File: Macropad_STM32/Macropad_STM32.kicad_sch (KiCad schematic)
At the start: 28 parts, among them J1 USB_C_Receptacle_USB2.0, J2 Conn_01x04_Pin, SW1 SW_Push, U1 STM32F103C8T6, U3 AMS1117-3.3, Y1 16MHz

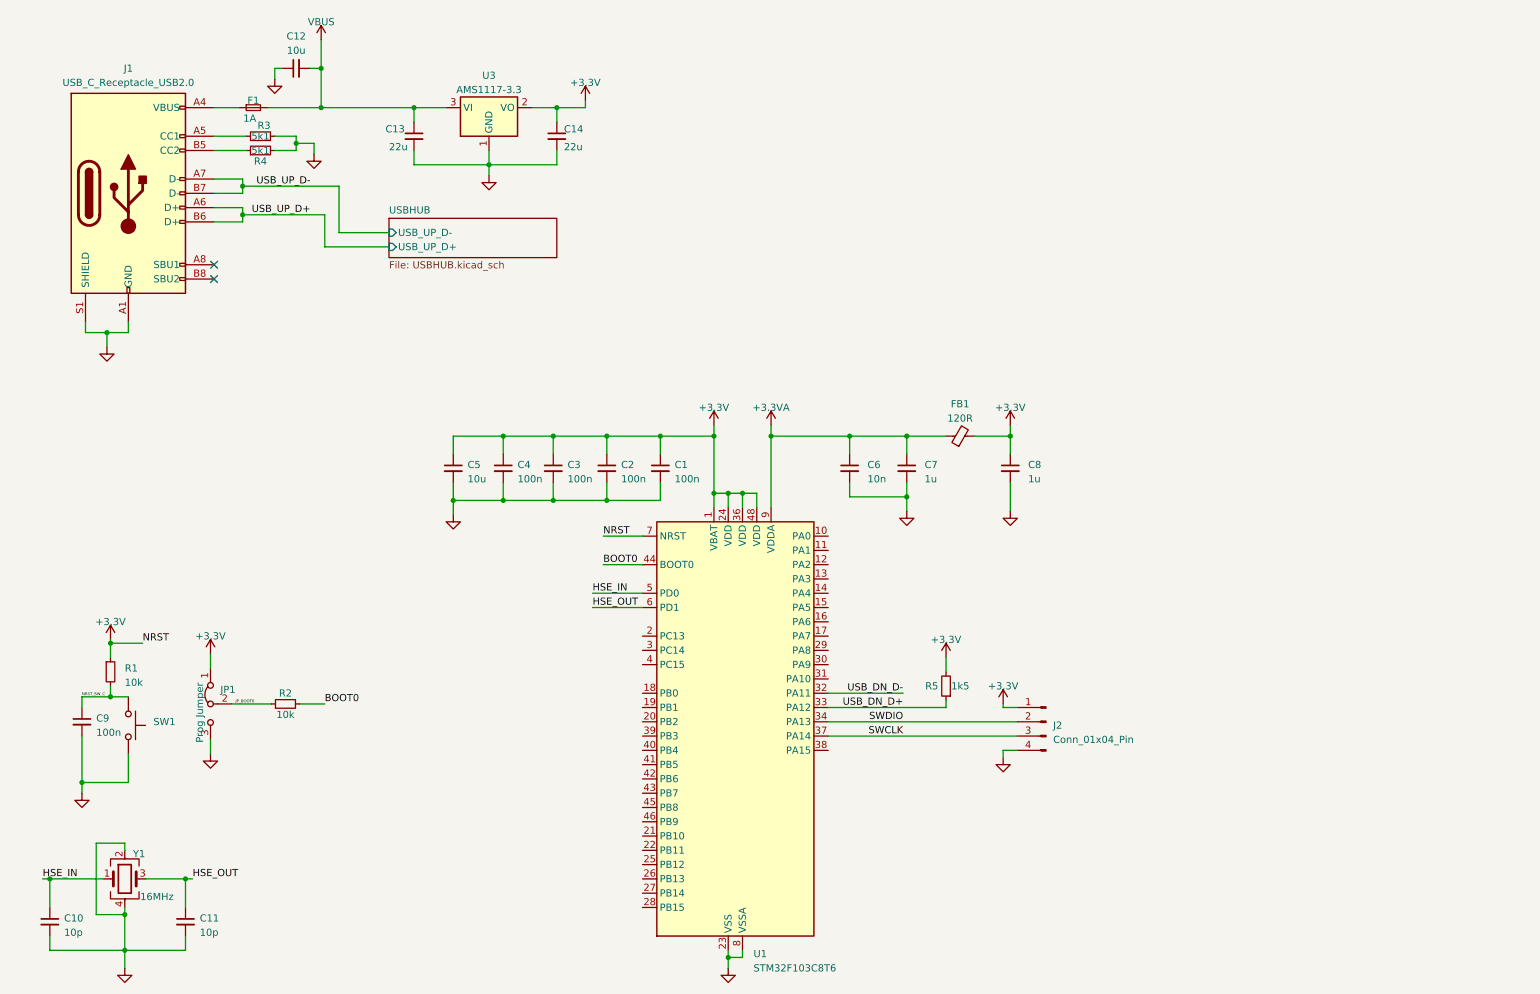
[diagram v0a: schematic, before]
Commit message: USB Hub & Jtag connectors added Todo: - Keypad matrix - Rotary encoders - PCB
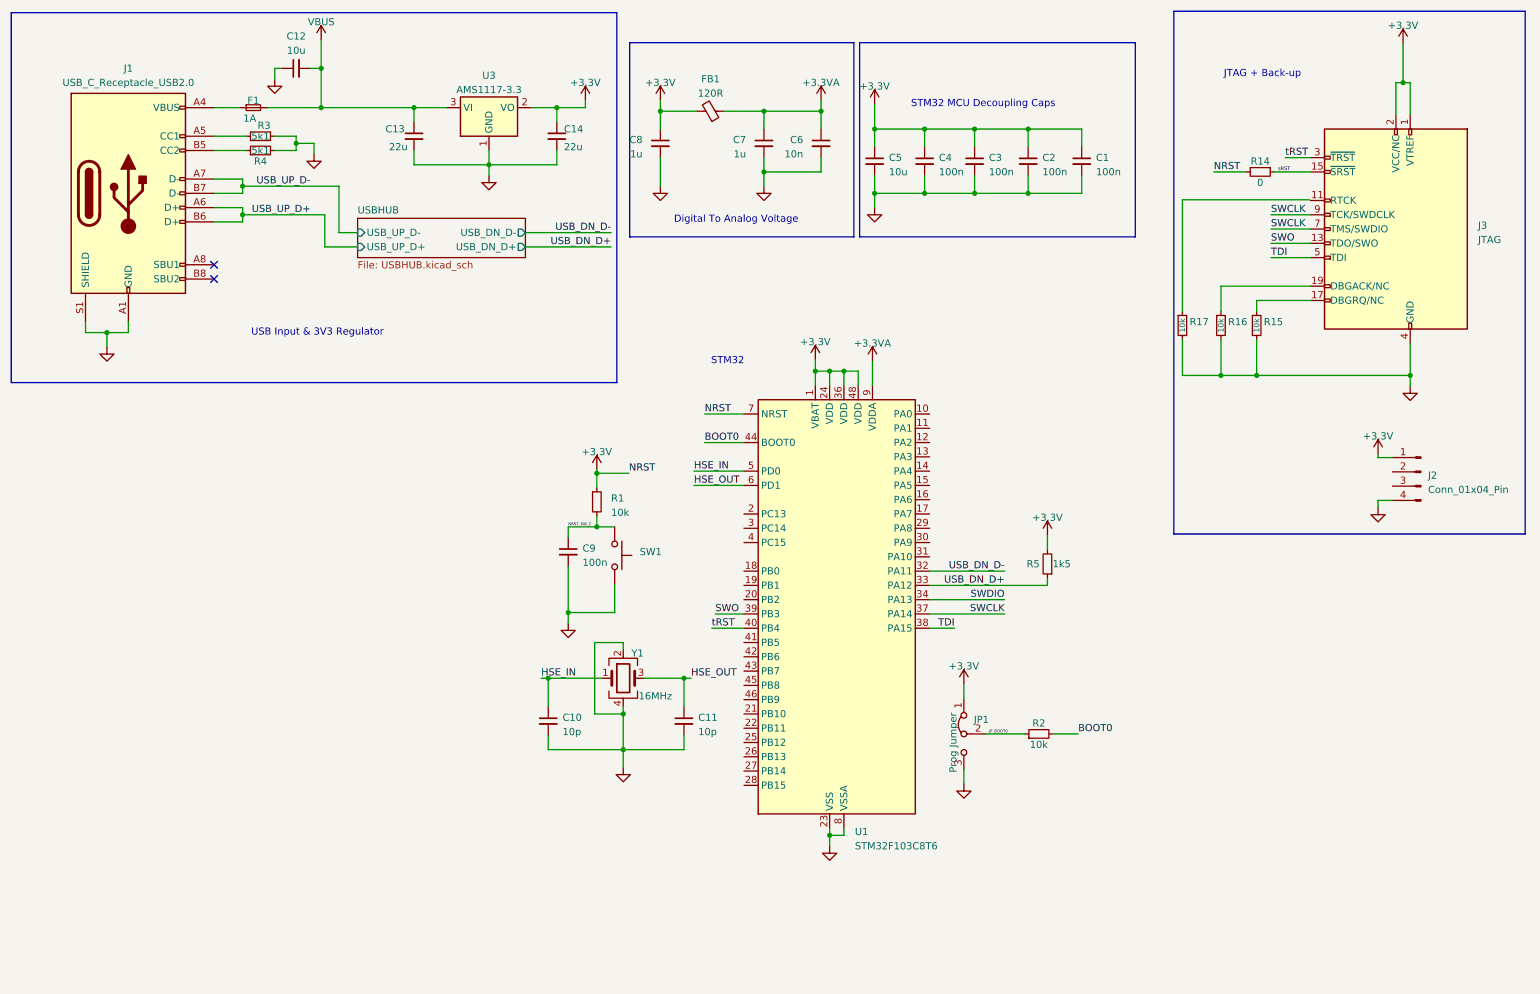
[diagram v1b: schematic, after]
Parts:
- added J3: JTAG, symbol Connector:Conn_ARM_JTAG_SWD_20
- added R14: 0, symbol Device:R_Small
- added R15, R16, R17: 10k, symbol Device:R_Small
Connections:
- net +3.3V: now also J3.1 (VTREF), J3.2 (VCC/NC), R14.2
- net GND: now also J3.10 (GND), J3.12 (GND), J3.14 (GND), J3.16 (GND), J3.18 (GND), J3.20 (GND), J3.4 (GND), J3.6 (GND), J3.8 (GND), R15.2, R16.2, R17.2
- net SWCLK: now also J3.7 (TMS/SWDIO), J3.9 (TCK/SWDCLK); no longer J2.3 (Pin_3)
- net SWDIO: no longer J2.2 (Pin_2)
- net TDI: now reaches U1.38 (PA15)
- net TDI: now also J3.5 (TDI)
- net SWO: now reaches U1.39 (PB3)
- net SWO: now also J3.13 (TDO/SWO)
- net tRST: now reaches U1.40 (PB4)
- net tRST: now also J3.3 (~{TRST})
- new net: J3.17 (DBGRQ/NC), R15.1
- new net: J3.19 (DBGACK/NC), R16.1
- new net sRST: J3.15 (~{SRST}), R14.1
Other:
- sheet USBHUB ports: added USB_DN_D+, USB_DN_D-; removed none
- note added: "Digital To Analog Voltage"
- note added: "JTAG + Back-up"
- note added: "STM32"
- note added: "STM32 MCU Decoupling Caps"
- note added: "USB Input & 3V3 Regulator"
- moved on the sheet: C1, C10, C11, C2, C3, C4, C5, C6, C7, C8, C9, FB1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

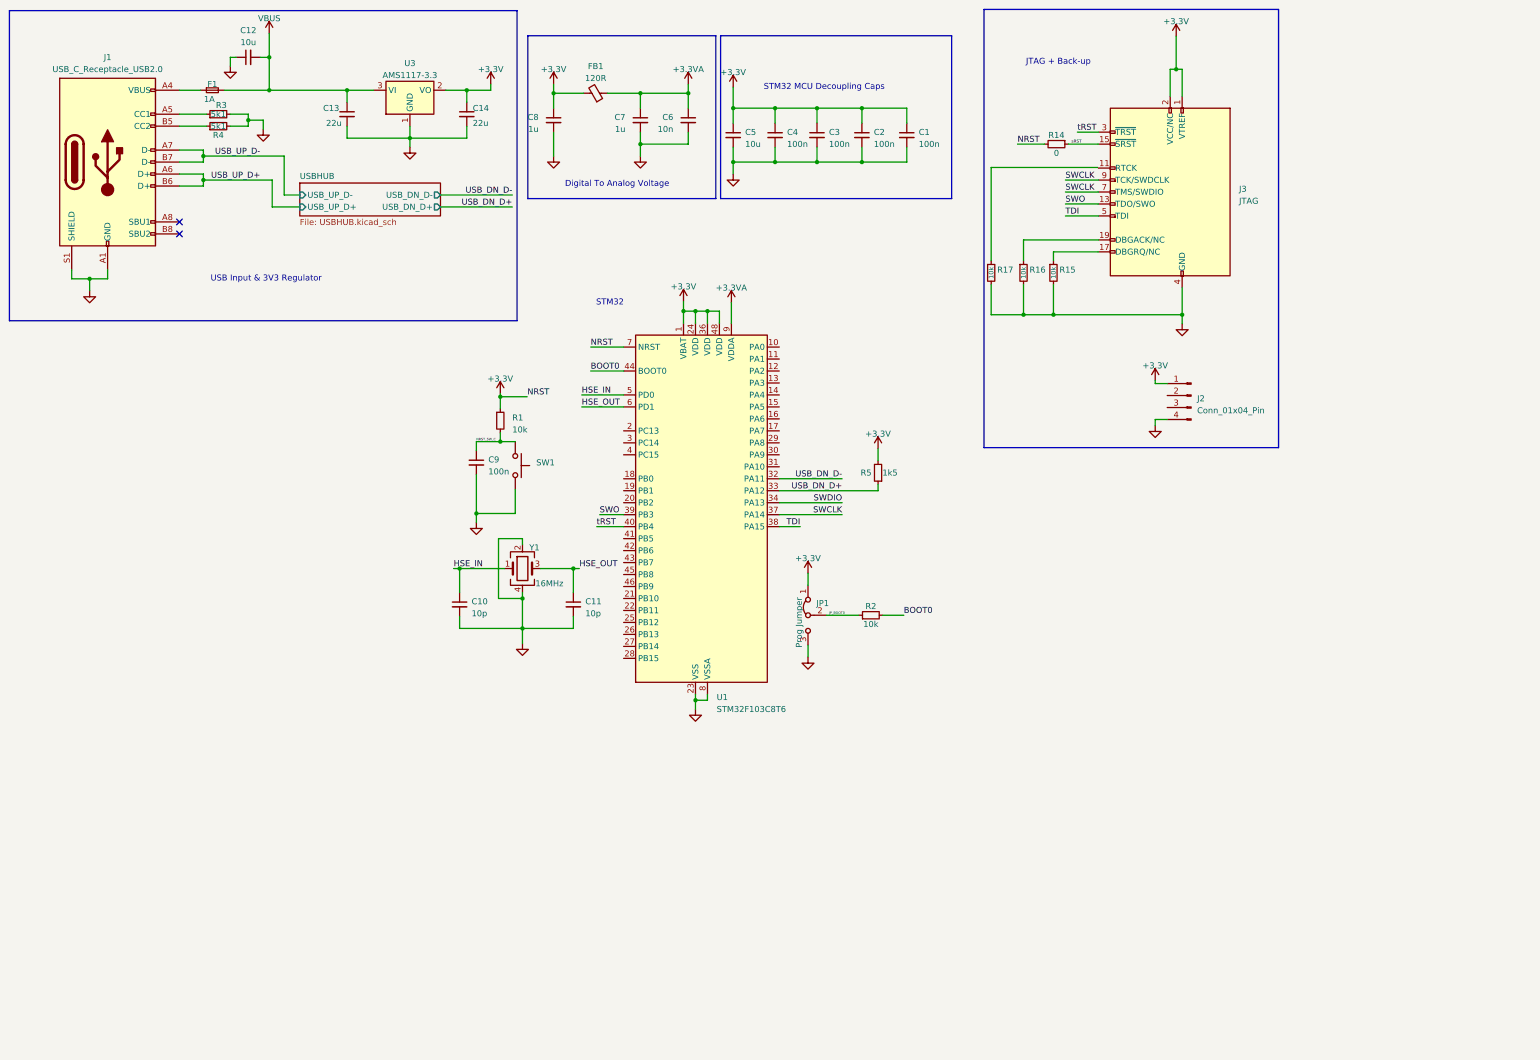
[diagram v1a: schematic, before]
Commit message: Finished main schematic (excl. matrix)
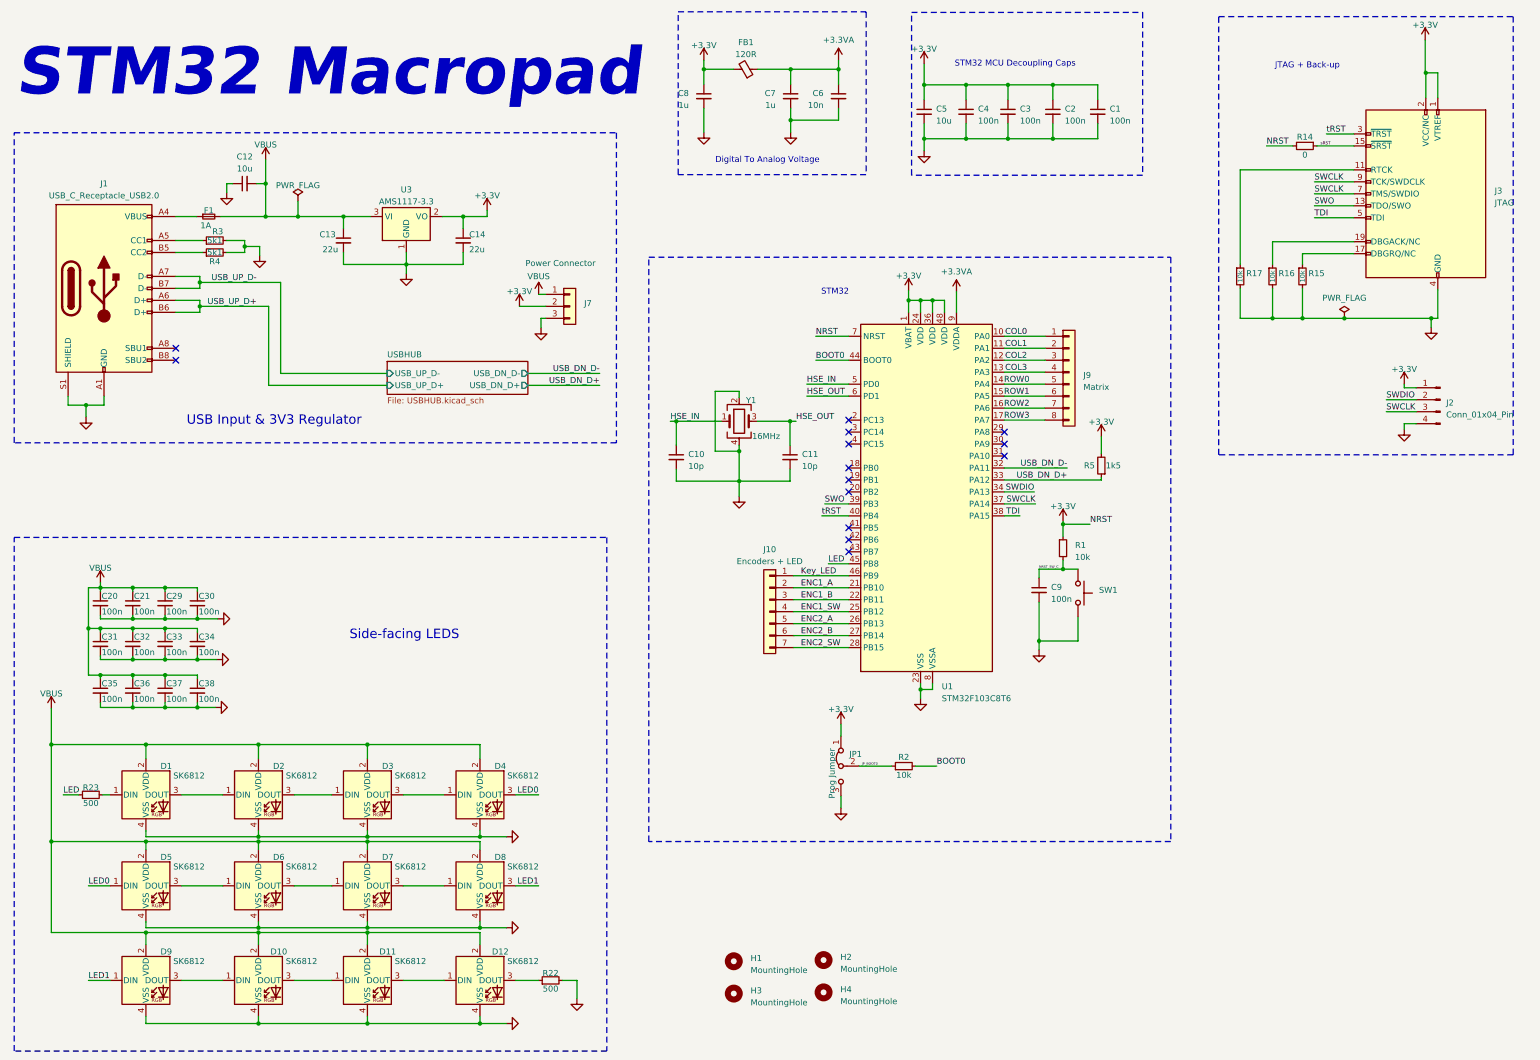
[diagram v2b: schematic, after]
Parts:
- added C20, C21, C29, C30, C31, C32, C33, C34, C35, C36, C37, C38: 100n, Capacitor_SMD:C_0805_2012Metric_Pad1.18x1.45mm_HandSolder, symbol Device:C_Small
- added D1, D10, D11, D12, D2, D3, D4, D5, D6, D7, D8, D9: SK6812, SK6812SIDE:SK6812SIDE, symbol LED:SK6812
- added H1, H2, H3, H4: MountingHole, MountingHole:MountingHole_3.2mm_M3_DIN965, symbol Mechanical:MountingHole
- added J10: Encoders + LED, Connector_JST:JST_EH_B7B-EH-A_1x07_P2.50mm_Vertical, symbol Connector_Generic:Conn_01x07
- added J7: Power Connector, Connector_JST:JST_EH_B3B-EH-A_1x03_P2.50mm_Vertical, symbol Connector_Generic:Conn_01x03
- added J9: Matrix, Connector_JST:JST_EH_B8B-EH-A_1x08_P2.50mm_Vertical, symbol Connector_Generic:Conn_01x08
- added R22, R23: 500, Resistor_SMD:R_0805_2012Metric_Pad1.20x1.40mm_HandSolder, symbol Device:R_Small
- C1, C10, C11, C12, C13, C14, C2, C3, C4, C5, C6, C7, C8, C9: footprint (none) -> Capacitor_SMD:C_0805_2012Metric_Pad1.18x1.45mm_HandSolder
- F1: footprint (none) -> Fuse:Fuse_1206_3216Metric_Pad1.42x1.75mm_HandSolder
- FB1: footprint (none) -> Fuse:Fuse_0805_2012Metric_Pad1.15x1.40mm_HandSolder
- J1: footprint (none) -> Connector_USB:USB_C_Receptacle_HRO_TYPE-C-31-M-12
- J2: footprint (none) -> Connector_PinHeader_2.54mm:PinHeader_1x04_P2.54mm_Vertical
- J3: footprint (none) -> Connector_PinHeader_2.54mm:PinHeader_2x10_P2.54mm_Vertical
- JP1: footprint (none) -> Connector_PinHeader_2.54mm:PinHeader_1x03_P2.54mm_Vertical
- R1, R14, R15, R16, R17, R2, R3, R4, R5: footprint (none) -> Resistor_SMD:R_0805_2012Metric_Pad1.20x1.40mm_HandSolder
- SW1: footprint (none) -> Button_Switch_SMD:SW_Tactile_SPST_NO_Straight_CK_PTS636Sx25SMTRLFS
- Y1: footprint (none) -> Crystal:Crystal_SMD_3225-4Pin_3.2x2.5mm_HandSoldering
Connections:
- net +3.3V: now also J7.2 (Pin_2); no longer C6.1, C7.1, FB1.1, U1.9 (VDDA)
- net GND: now also C20.2, C21.2, C29.2, C30.2, C31.2, C32.2, C33.2, C34.2, C35.2, C36.2, C37.2, C38.2, D1.4 (VSS), D10.4 (VSS), D11.4 (VSS), D12.4 (VSS), D2.4 (VSS), D3.4 (VSS), D4.4 (VSS), D5.4 (VSS), D6.4 (VSS), D7.4 (VSS), D8.4 (VSS), D9.4 (VSS), J7.3 (Pin_3), R22.2
- net SWCLK: now also J2.3 (Pin_3)
- net SWDIO: now also J2.2 (Pin_2)
- net VBUS: now also C20.1, C21.1, C29.1, C30.1, C31.1, C32.1, C33.1, C34.1, C35.1, C36.1, C37.1, C38.1, D1.2 (VDD), D10.2 (VDD), D11.2 (VDD), D12.2 (VDD), D2.2 (VDD), D3.2 (VDD), D4.2 (VDD), D5.2 (VDD), D6.2 (VDD), D7.2 (VDD), D8.2 (VDD), D9.2 (VDD), J7.1 (Pin_1)
- net at J3.11 (RTCK): now also R17.1
- net COL0: now reaches U1.10 (PA0)
- net COL0: now also J9.1 (Pin_1)
- net COL1: now reaches U1.11 (PA1)
- net COL1: now also J9.2 (Pin_2)
- net COL2: now reaches U1.12 (PA2)
- net COL2: now also J9.3 (Pin_3)
- net COL3: now reaches U1.13 (PA3)
- net COL3: now also J9.4 (Pin_4)
- net ROW0: now reaches U1.14 (PA4)
- net ROW0: now also J9.5 (Pin_5)
- net ROW1: now reaches U1.15 (PA5)
- net ROW1: now also J9.6 (Pin_6)
- net ROW2: now reaches U1.16 (PA6)
- net ROW2: now also J9.7 (Pin_7)
- net ROW3: now reaches U1.17 (PA7)
- net ROW3: now also J9.8 (Pin_8)
- net ENC1_A: now reaches U1.21 (PB10)
- net ENC1_A: now also J10.2 (Pin_2)
- net ENC1_B: now reaches U1.22 (PB11)
- net ENC1_B: now also J10.3 (Pin_3)
- net ENC1_SW: now reaches U1.25 (PB12)
- net ENC1_SW: now also J10.4 (Pin_4)
- net ENC2_A: now reaches U1.26 (PB13)
- net ENC2_A: now also J10.5 (Pin_5)
- net ENC2_B: now reaches U1.27 (PB14)
- net ENC2_B: now also J10.6 (Pin_6)
- net ENC2_SW: now reaches U1.28 (PB15)
- net ENC2_SW: now also J10.7 (Pin_7)
- net LED: now reaches U1.45 (PB8)
- net LED: now also R23.1
- net Key_LED: now reaches U1.46 (PB9)
- net Key_LED: now also J10.1 (Pin_1)
- new net: D5.3 (DOUT), D6.1 (DIN)
- new net: D12.3 (DOUT), R22.1
- new net: D1.1 (DIN), R23.2
- new net: D1.3 (DOUT), D2.1 (DIN)
- new net: D6.3 (DOUT), D7.1 (DIN)
- new net: D2.3 (DOUT), D3.1 (DIN)
- new net: D3.3 (DOUT), D4.1 (DIN)
- new net: D11.3 (DOUT), D12.1 (DIN)
- new net: D10.1 (DIN), D9.3 (DOUT)
- new net: D10.3 (DOUT), D11.1 (DIN)
- new net: D7.3 (DOUT), D8.1 (DIN)
- new net +3.3VA: C6.1, C7.1, FB1.1, U1.9 (VDDA)
- new net LED0: D4.3 (DOUT), D5.1 (DIN)
- new net LED1: D8.3 (DOUT), D9.1 (DIN)
- no-connect marks 2 -> 14
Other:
- note added: "STM32 Macropad"
- note added: "Side-facing LEDS"
- title: (none) -> STM32 Macropad
- moved on the sheet: C1, C10, C11, C12, C13, C14, C2, C3, C4, C5, C6, C7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

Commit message: Matrix PCB layout done
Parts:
- added H5, H6, H7, H8: MountingHole, MountingHole:MountingHole_3.2mm_M3_DIN965, symbol Mechanical:MountingHole
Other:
- added sheet Matrix (matrix.kicad_sch)
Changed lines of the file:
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@@
+    )
+  )
+  (symbol (lib_id "Mechanical:MountingHole") (at 168.656 205.74 0) (unit 1)
+    (in_bom yes) (on_board yes) (dnp no) (fields_autoplaced)
+    (property "Reference" "H6" (at 172.212 205.105 0)
+      (effects (font (size 1.27 1.27)) (justify left))
+    )
+    (property "Value" "MountingHole" (at 172.212 207.645 0)
+      (effects (font (size 1.27 1.27)) (justify left))
+    )
+    (property "Footprint" "MountingHole:MountingHole_3.2mm_M3_DIN965" (at 168.656 205.74 0)
+      (effects (font (size 1.27 1.27)) hide)
+    )
+    (property "Datasheet" "~" (at 168.656 205.74 0)
+      (effects (font (size 1.27 1.27)) hide)
+    )
+    (instances
+      (project "Macropad_STM32"
+        (path "/1bbb8170-4e2d-4119-974a-402fa0f6f9bf"
+          (reference "H6") (unit 1)
+        )
+      )
     )
   )
@@
         (path "/1bbb8170-4e2d-4119-974a-402fa0f6f9bf"
           (reference "#PWR01") (unit 1)
+        )
+      )
+    )
+  )
+  (symbol (lib_id "Mechanical:MountingHole") (at 187.706 198.628 0) (unit 1)
+    (in_bom yes) (on_board yes) (dnp no) (fields_autoplaced)
+    (property "Reference" "H7" (at 191.262 197.993 0)
+      (effects (font (size 1.27 1.27)) (justify left))
+    )
+    (property "Value" "MountingHole" (at 191.262 200.533 0)
+      (effects (font (size 1.27 1.27)) (justify left))
+    )
+    (property "Footprint" "MountingHole:MountingHole_3.2mm_M3_DIN965" (at 187.706 198.628 0)
+      (effects (font (size 1.27 1.27)) hide)
+    )
+    (property "Datasheet" "~" (at 187.706 198.628 0)
+      (effects (font (size 1.27 1.27)) hide)
+    )
+    (instances
+      (project "Macropad_STM32"
+        (path "/1bbb8170-4e2d-4119-974a-402fa0f6f9bf"
+          (reference "H7") (unit 1)
         )
       )
@@
     )
   )
+  (symbol (lib_id "Mechanical:MountingHole") (at 187.706 205.486 0) (unit 1)
+    (in_bom yes) (on_board yes) (dnp no) (fields_autoplaced)
+    (property "Reference" "H8" (at 191.262 204.851 0)
+      (effects (font (size 1.27 1.27)) (justify left))
+    )
+    (property "Value" "MountingHole" (at 191.262 207.391 0)
+      (effects (font (size 1.27 1.27)) (justify left))
+    )
+    (property "Footprint" "MountingHole:MountingHole_3.2mm_M3_DIN965" (at 187.706 205.486 0)
+      (effects (font (size 1.27 1.27)) hide)
+    )
+    (property "Datasheet" "~" (at 187.706 205.486 0)
+      (effects (font (size 1.27 1.27)) hide)
+    )
+    (instances
+      (project "Macropad_STM32"
+        (path "/1bbb8170-4e2d-4119-974a-402fa0f6f9bf"
+          (reference "H8") (unit 1)
+        )
+      )
+    )
+  )
   (symbol (lib_id "power:VBUS") (at 23.622 161.036 0) (unit 1)
     (in_bom yes) (on_board yes) (dnp no) (fields_autoplaced)
@@
         (path "/1bbb8170-4e2d-4119-974a-402fa0f6f9bf"
           (reference "C13") (unit 1)
+        )
+      )
+    )
+  )
+  (symbol (lib_id "Mechanical:MountingHole") (at 168.656 198.882 0) (unit 1)
+    (in_bom yes) (on_board yes) (dnp no) (fields_autoplaced)
+    (property "Reference" "H5" (at 172.212 198.247 0)
+      (effects (font (size 1.27 1.27)) (justify left))
+    )
+    (property "Value" "MountingHole" (at 172.212 200.787 0)
+      (effects (font (size 1.27 1.27)) (justify left))
+    )
+    (property "Footprint" "MountingHole:MountingHole_3.2mm_M3_DIN965" (at 168.656 198.882 0)
+      (effects (font (size 1.27 1.27)) hide)
+    )
+    (property "Datasheet" "~" (at 168.656 198.882 0)
+      (effects (font (size 1.27 1.27)) hide)
+    )
+    (instances
+      (project "Macropad_STM32"
+        (path "/1bbb8170-4e2d-4119-974a-402fa0f6f9bf"
+          (reference "H5") (unit 1)
         )
       )
@@
       )
     )
+  )
+  (sheet (at 272.288 137.922) (size 60.706 37.846) (fields_autoplaced)
+    (stroke (width 0.1524) (type solid))
+    (fill (color 0 0 0 0.0000))
+    (property "Sheetname" "Matrix" (at 272.288 137.2104 0)
+      (effects (font (size 1.27 1.27)) (justify left bottom))
+    )
+    (property "Sheetfile" "matrix.kicad_sch" (at 272.288 176.3526 0)
+      (effects (font (size 1.27 1.27)) (justify left top))
+    )
+    (instances
+      (project "Macropad_STM32"
+        (path "/1bbb8170-4e2d-4119-974a-402fa0f6f9bf" (page "3"))
+      )
+    )
